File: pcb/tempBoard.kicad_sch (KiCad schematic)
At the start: 6 parts, among them J1 OLED_128X64_1.3_I2C, U1 SHTC3, U2 XIAO-RP2040-DIP

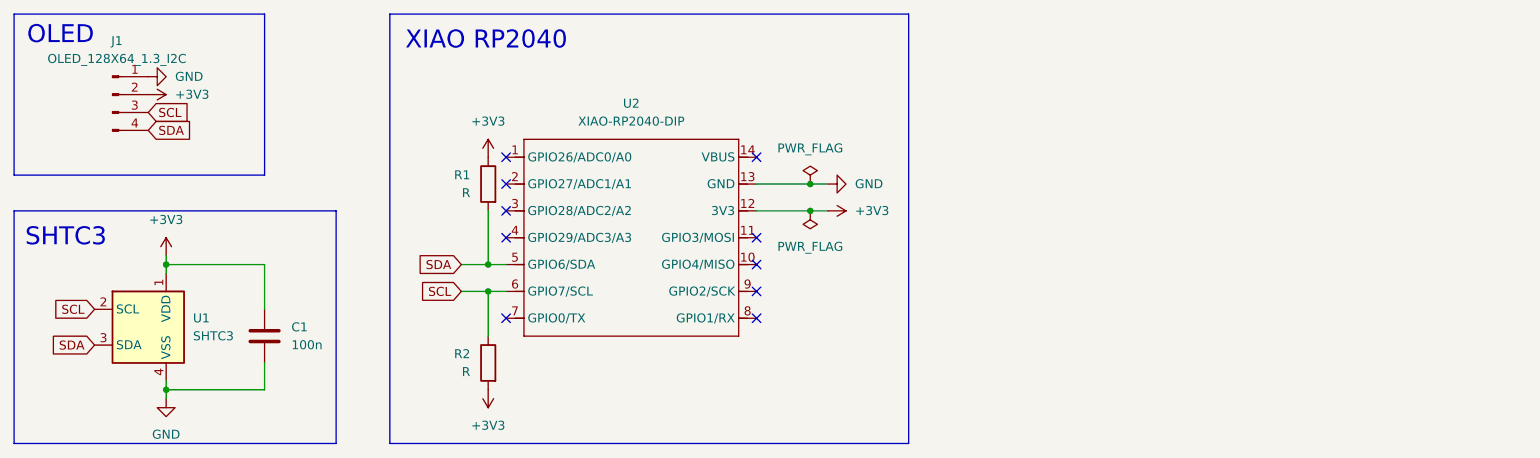
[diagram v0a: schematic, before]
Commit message: added indicator lights
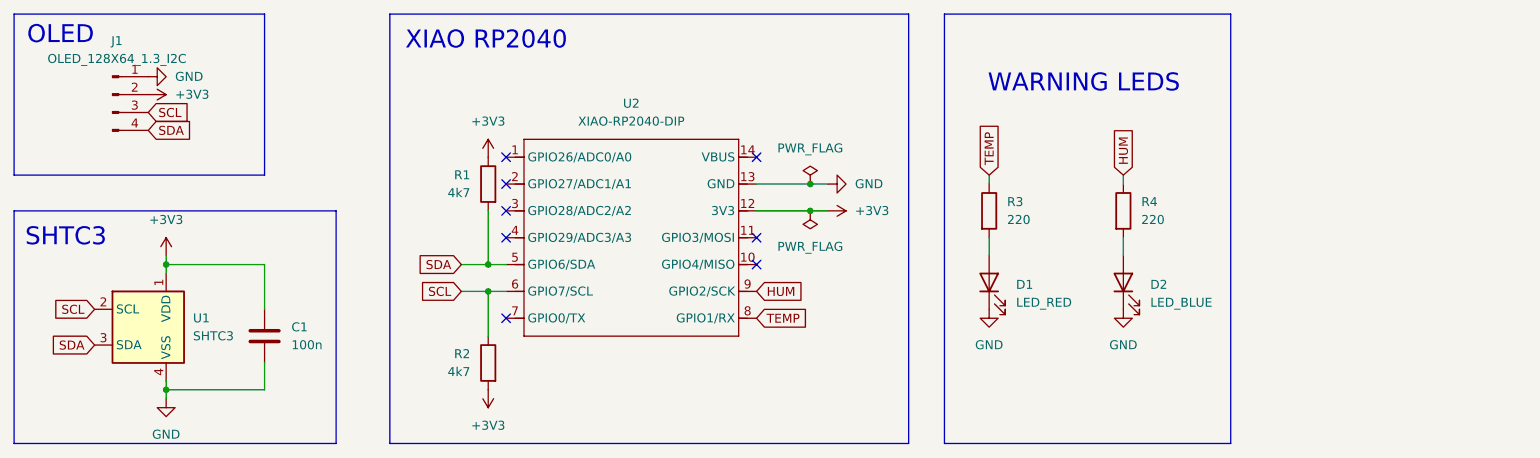
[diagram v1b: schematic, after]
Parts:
- added D1: LED_RED, LED_SMD:LED_1206_3216Metric, symbol Device:LED
- added D2: LED_BLUE, LED_SMD:LED_1206_3216Metric, symbol Device:LED
- added R3, R4: 220, Resistor_SMD:R_0805_2012Metric, symbol Device:R
- R1, R2: value R -> 4k7
- U1: footprint Sensor_Humidity:Sensirion_DFN-4-1EP_2x2mm_P1mm_EP0.7x1.6mm -> general:Sensirion_DFN-4-1EP_2x2mm_P1mm_EP0.7x1.6mm
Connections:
- net GND: now also D1.1 (K), D2.1 (K)
- net TEMP: now reaches U2.8 (GPIO1/RX)
- net TEMP: now also R3.1
- net HUM: now reaches U2.9 (GPIO2/SCK)
- net HUM: now also R4.1
- new net: D2.2 (A), R4.2
- new net: D1.2 (A), R3.2
- no-connect marks 10 -> 8
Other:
- note added: "WARNING LEDS"

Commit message: update readme
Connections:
- net GND: now also U1.5 (VSS)
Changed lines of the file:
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@@
+	(wire
+		(pts
+			(xy 85.09 99.06) (xy 87.63 99.06)
+		)
+		(stroke
+			(width 0)
+			(type default)
+		)
+	)
 	(wire
 		(pts
@@
 		(pts
 			(xy 87.63 97.79) (xy 87.63 99.06)
+		)
+		(stroke
+			(width 0)
+			(type default)
+		)
+	)
+	(wire
+		(pts
+			(xy 85.09 97.79) (xy 85.09 99.06)
 		)
 		(stroke
@@
 		(pin "2"
 		)
+		(pin "5"
+		)
 		(instances

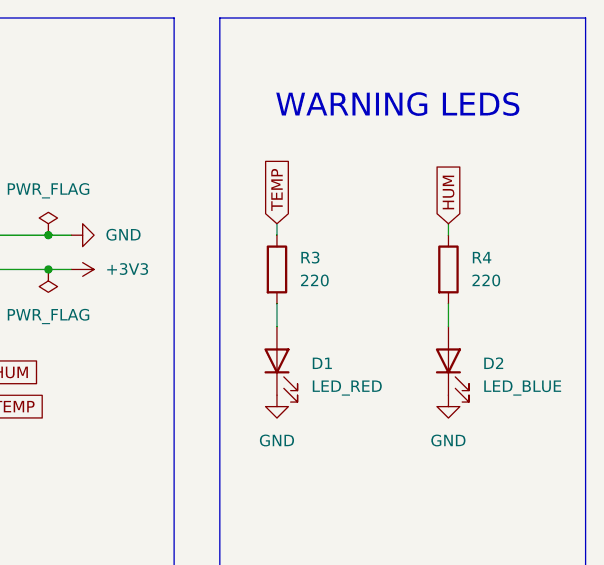
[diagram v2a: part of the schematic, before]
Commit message: remake production files + lcsc part number fields
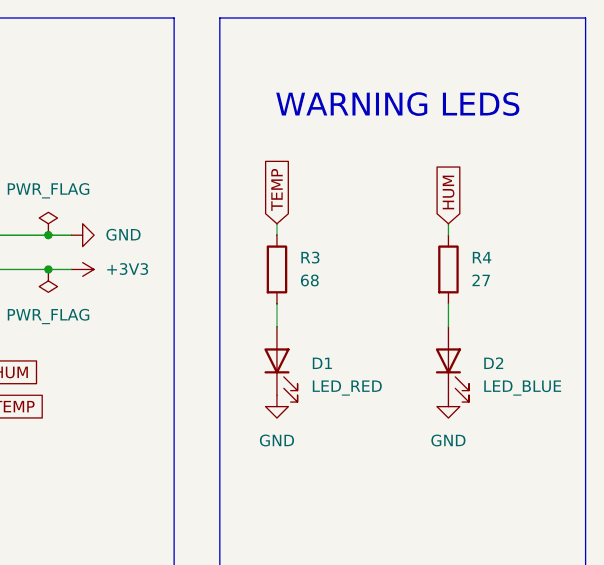
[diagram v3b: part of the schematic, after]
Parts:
- R3: value 220 -> 68
- R4: value 220 -> 27
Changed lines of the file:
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@@
 			)
 		)
-		(property "Value" "220"
+		(property "Value" "27"
 			(at 226.06 74.9299 0)
 			(effects
@@
 			)
 		)
-		(property "Value" "220"
+		(property "Value" "68"
 			(at 207.01 74.9299 0)
 			(effects

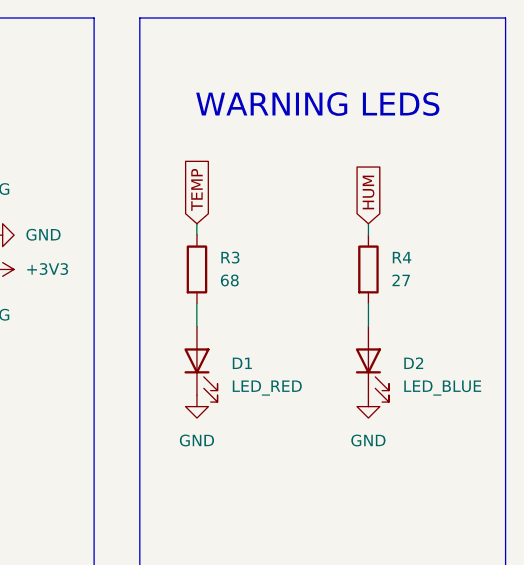
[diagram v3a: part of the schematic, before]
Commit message: fix some dfm errors
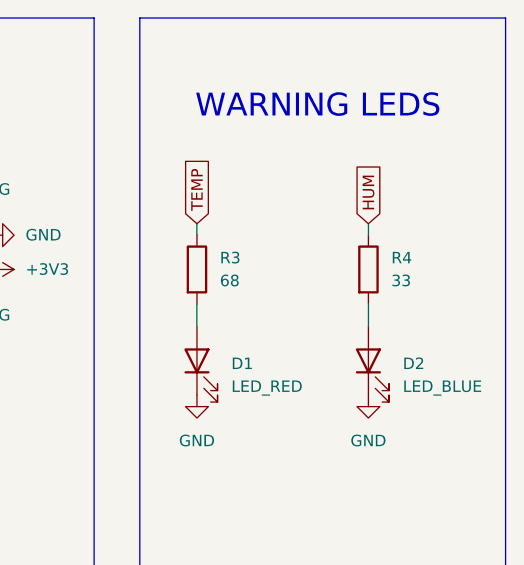
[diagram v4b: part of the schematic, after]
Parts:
- R4: value 27 -> 33
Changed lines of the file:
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@@
 			)
 		)
-		(property "Value" "27"
+		(property "Value" "33"
 			(at 226.06 74.9299 0)
 			(effects

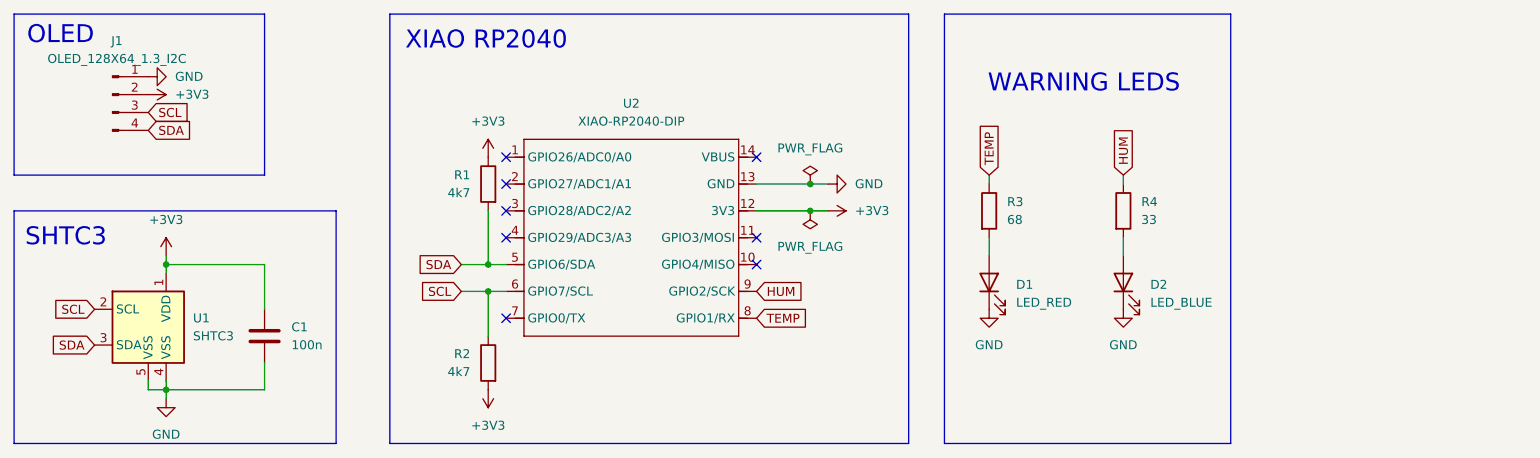
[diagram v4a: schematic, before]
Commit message: update pullups
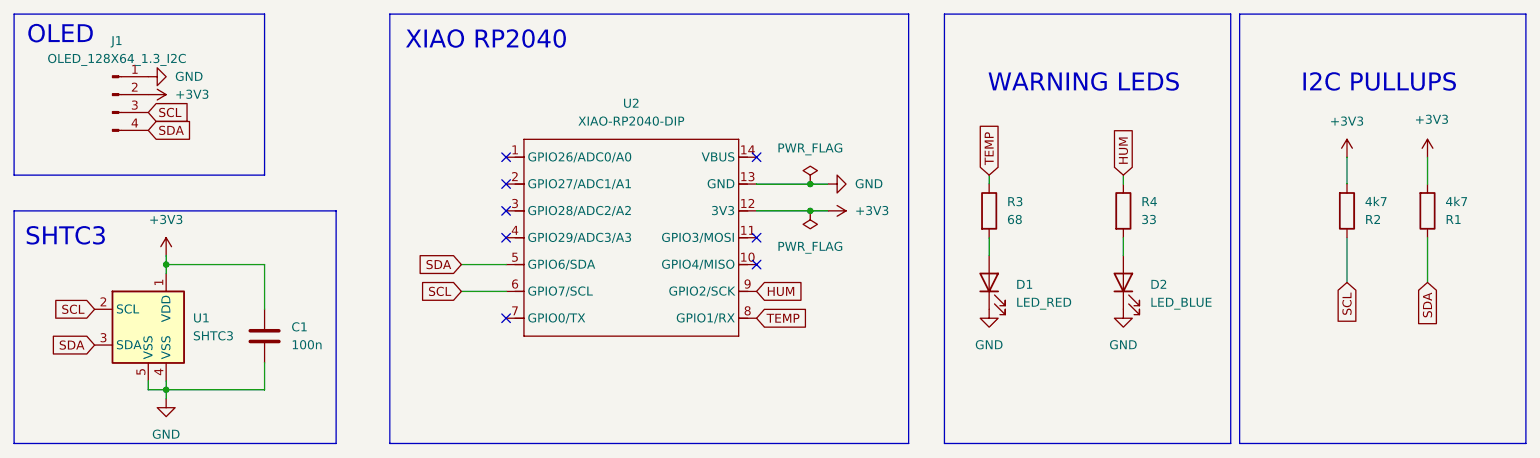
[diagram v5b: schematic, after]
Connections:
- net +3V3: now also R1.2; no longer R1.1
- net SDA: now also R1.1; no longer R1.2
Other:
- note added: "I2C PULLUPS"
- moved on the sheet: R1, R2
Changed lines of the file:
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@@
-	)
-	(junction
-		(at 133.35 85.09)
-		(diameter 0)
-		(color 0 0 0 0)
 	)
 	(junction
@@
 		(color 0 0 0 0)
 	)
-	(junction
-		(at 133.35 81.28)
-		(diameter 0)
-		(color 0 0 0 0)
-	)
 	(no_connect
 		(at 135.89 73.66)
@@
 	(wire
 		(pts
+			(xy 266.7 66.04) (xy 266.7 69.85)
+		)
+		(stroke
+			(width 0)
+			(type default)
+		)
+	)
+	(wire
+		(pts
 			(xy 204.47 77.47) (xy 204.47 80.01)
 		)
@@
 	(wire
 		(pts
-			(xy 133.35 81.28) (xy 135.89 81.28)
-		)
-		(stroke
-			(width 0)
-			(type default)
-		)
-	)
-	(wire
-		(pts
 			(xy 101.6 95.25) (xy 101.6 99.06)
 		)
@@
 	(wire
 		(pts
-			(xy 129.54 85.09) (xy 133.35 85.09)
-		)
-		(stroke
-			(width 0)
-			(type default)
-		)
-	)
-	(wire
-		(pts
-			(xy 133.35 91.44) (xy 133.35 85.09)
+			(xy 255.27 77.47) (xy 255.27 83.82)
+		)
+		(stroke
+			(width 0)
+			(type default)
+		)
+	)
+	(wire
+		(pts
+			(xy 266.7 83.82) (xy 266.7 77.47)
 		)
 		(stroke
@@
 	(wire
 		(pts
-			(xy 133.35 85.09) (xy 135.89 85.09)
+			(xy 129.54 85.09) (xy 135.89 85.09)
 		)
 		(stroke
@@
 	(wire
 		(pts
-			(xy 133.35 73.66) (xy 133.35 81.28)
-		)
-		(stroke
-			(width 0)
-			(type default)
-		)
-	)
-	(wire
-		(pts
 			(xy 223.52 77.47) (xy 223.52 80.01)
 		)
@@
 	(wire
 		(pts
-			(xy 129.54 81.28) (xy 133.35 81.28)
+			(xy 129.54 81.28) (xy 135.89 81.28)
 		)
 		(stroke
@@
 		(pts
 			(xy 87.63 81.28) (xy 87.63 82.55)
+		)
+		(stroke
+			(width 0)
+			(type default)
+		)
+	)
+	(wire
+		(pts
+			(xy 255.27 66.04) (xy 255.27 69.85)
 		)
 		(stroke
@@
 		(start 66.04 73.66)
 		(end 111.76 106.68)
+		(stroke
+			(width 0)
+			(type default)
+		)
+		(fill
+			(type none)
+		)
+	)
+	(rectangle
+		(start 240.03 45.72)
+		(end 280.67 106.68)
 		(stroke
 			(width 0)
@@
 		)
 	)
+	(text "I2C PULLUPS"
+		(exclude_from_sim no)
+		(at 259.842 55.626 0)
+		(effects
+			(font
+				(face "KiCad Font")
+				(size 2.54 2.54)
+				(thickness 0.3175)
+			)
+		)
+	)
 	(global_label "SCL"
 		(shape input)
@@
 		)
 	)
+	(global_label "SCL"
+		(shape input)
+		(at 255.27 83.82 270)
+		(fields_autoplaced yes)
+		(effects
+			(font
+				(size 1.27 1.27)
+			)
+			(justify right)
+		)
+		(property "Intersheetrefs" "${INTERSHEET_REFS}"
+			(at 255.27 90.3128 90)
+			(effects
+				(font
+					(size 1.27 1.27)
+				)
+				(justify right)
+				(hide yes)
+			)
+		)
+	)
 	(global_label "TEMP"
 		(shape input)
@@
 		(property "Intersheetrefs" "${INTERSHEET_REFS}"
 			(at 70.9167 92.71 0)
+			(effects
+				(font
+					(size 1.27 1.27)
+				)
+				(justify right)
+				(hide yes)
+			)
+		)
+	)
+	(global_label "SDA"
+		(shape input)
+		(at 266.7 83.82 270)
+		(fields_autoplaced yes)
+		(effects
+			(font
+				(size 1.27 1.27)
+			)
+			(justify right)
+		)
+		(property "Intersheetrefs" "${INTERSHEET_REFS}"
+			(at 266.7 90.3733 90)
 			(effects
 				(font
@@
 	(symbol
 		(lib_id "power:+3V3")
-		(at 133.35 99.06 180)
+		(at 255.27 66.04 0)
 		(unit 1)
 		(exclude_from_sim no)
@@
 		(fields_autoplaced yes)
 		(property "Reference" "#PWR06"
-			(at 133.35 95.25 0)
+			(at 255.27 69.85 0)
 			(effects
 				(font
@@
 		)
 		(property "Value" "+3V3"
-			(at 133.35 104.14 0)
+			(at 255.27 60.96 0)
 			(effects
 				(font
@@
 		)
 		(property "Footprint" ""
-			(at 133.35 99.06 0)
+			(at 255.27 66.04 0)
 			(effects
 				(font
@@
 		)
 		(property "Datasheet" ""
-			(at 133.35 99.06 0)
+			(at 255.27 66.04 0)
 			(effects
 				(font
@@
 		)
 		(property "Description" "Power symbol creates a global label with name \"+3V3\""
-			(at 133.35 99.06 0)
+			(at 255.27 66.04 0)
 			(effects
 				(font
@@
 	(symbol
 		(lib_id "Device:R")
-		(at 133.35 69.85 0)
-		(mirror y)
+		(at 266.7 73.66 0)
+		(mirror x)
 		(unit 1)
 		(exclude_from_sim no)
@@
 		(fields_autoplaced yes)
 		(property "Reference" "R1"
-			(at 130.81 68.5799 0)
+			(at 269.24 74.9301 0)
 			(effects
 				(font
@@
 		)
 		(property "Value" "4k7"
-			(at 130.81 71.1199 0)
+			(at 269.24 72.3901 0)
 			(effects
 				(font
@@
 		)
 		(property "Footprint" "Resistor_SMD:R_0805_2012Metric"
-			(at 135.128 69.85 90)
+			(at 264.922 73.66 90)
 			(effects
 				(font
@@
 		)
 		(property "Datasheet" "~"
-			(at 133.35 69.85 0)
+			(at 266.7 73.66 0)
 			(effects
 				(font
@@
 		)
 		(property "Description" "Resistor"
-			(at 133.35 69.85 0)
+			(at 266.7 73.66 0)
 			(effects
 				(font
@@
 	(symbol
 		(lib_id "power:+3V3")
-		(at 133.35 66.04 0)
+		(at 266.7 66.04 0)
 		(unit 1)
 		(exclude_from_sim no)
@@
 		(on_board yes)
 		(dnp no)
-		(fields_autoplaced yes)
 		(property "Reference" "#PWR05"
-			(at 133.35 69.85 0)
+			(at 266.7 69.85 0)
 			(effects
 				(font
@@
 		)
 		(property "Value" "+3V3"
-			(at 133.35 60.96 0)
-			(effects
-				(font
-					(size 1.27 1.27)
-				)
+			(at 269.748 60.706 0)
+			(effects
+				(font
+					(size 1.27 1.27)
+				)
+				(justify right)
 			)
 		)
 		(property "Footprint" ""
-			(at 133.35 66.04 0)
+			(at 266.7 66.04 0)
 			(effects
 				(font
@@
 		)
 		(property "Datasheet" ""
-			(at 133.35 66.04 0)
+			(at 266.7 66.04 0)
 			(effects
 				(font
@@
 		)
 		(property "Description" "Power symbol creates a global label with name \"+3V3\""
-			(at 133.35 66.04 0)
+			(at 266.7 66.04 0)
 			(effects
 				(font
@@
 	(symbol
 		(lib_id "Device:R")
-		(at 133.35 95.25 0)
-		(mirror y)
+		(at 255.27 73.66 0)
+		(mirror x)
 		(unit 1)
 		(exclude_from_sim no)
@@
 		(fields_autoplaced yes)
 		(property "Reference" "R2"
-			(at 130.81 93.9799 0)
+			(at 257.81 74.9301 0)
 			(effects
 				(font
@@
 		)
 		(property "Value" "4k7"
-			(at 130.81 96.5199 0)
+			(at 257.81 72.3901 0)
 			(effects
 				(font
@@
 		)
 		(property "Footprint" "Resistor_SMD:R_0805_2012Metric"
-			(at 135.128 95.25 90)
+			(at 253.492 73.66 90)
 			(effects
 				(font
@@
 		)
 		(property "Datasheet" "~"
-			(at 133.35 95.25 0)
+			(at 255.27 73.66 0)
 			(effects
 				(font
@@
 		)
 		(property "Description" "Resistor"
-			(at 133.35 95.25 0)
-			(effects
-				(font
+			(at 255.27 73.66 0)
+			(effects
+				(font

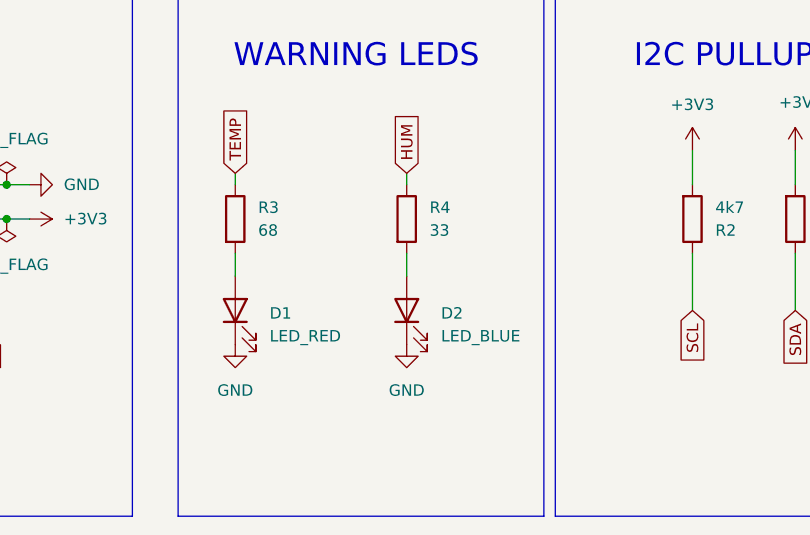
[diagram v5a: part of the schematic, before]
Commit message: make jlc cheaper
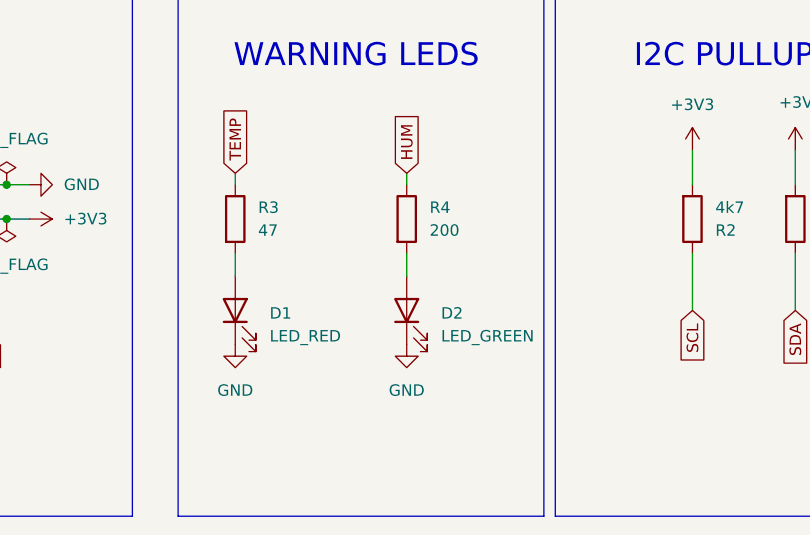
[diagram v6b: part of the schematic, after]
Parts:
- D1: footprint LED_SMD:LED_1206_3216Metric -> LED_SMD:LED_0805_2012Metric
- D2: value LED_BLUE -> LED_GREEN; footprint LED_SMD:LED_1206_3216Metric -> LED_SMD:LED_0805_2012Metric
- R3: value 68 -> 47
- R4: value 33 -> 200
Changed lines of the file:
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@@
 			)
 		)
-		(property "Value" "33"
+		(property "Value" "200"
 			(at 226.06 74.9299 0)
 			(effects
@@
 			)
 		)
-		(property "Value" "LED_BLUE"
+		(property "Value" "LED_GREEN"
 			(at 227.33 86.6774 90)
 			(effects
@@
 			)
 		)
-		(property "Footprint" "LED_SMD:LED_1206_3216Metric"
+		(property "Footprint" "LED_SMD:LED_0805_2012Metric"
 			(at 223.52 83.82 0)
 			(effects
@@
 			)
 		)
-		(property "Value" "68"
+		(property "Value" "47"
 			(at 207.01 74.9299 0)
 			(effects
@@
 			)
 		)
-		(property "Footprint" "LED_SMD:LED_1206_3216Metric"
+		(property "Footprint" "LED_SMD:LED_0805_2012Metric"
 			(at 204.47 83.82 0)
 			(effects
